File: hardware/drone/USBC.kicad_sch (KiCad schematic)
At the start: 8 parts

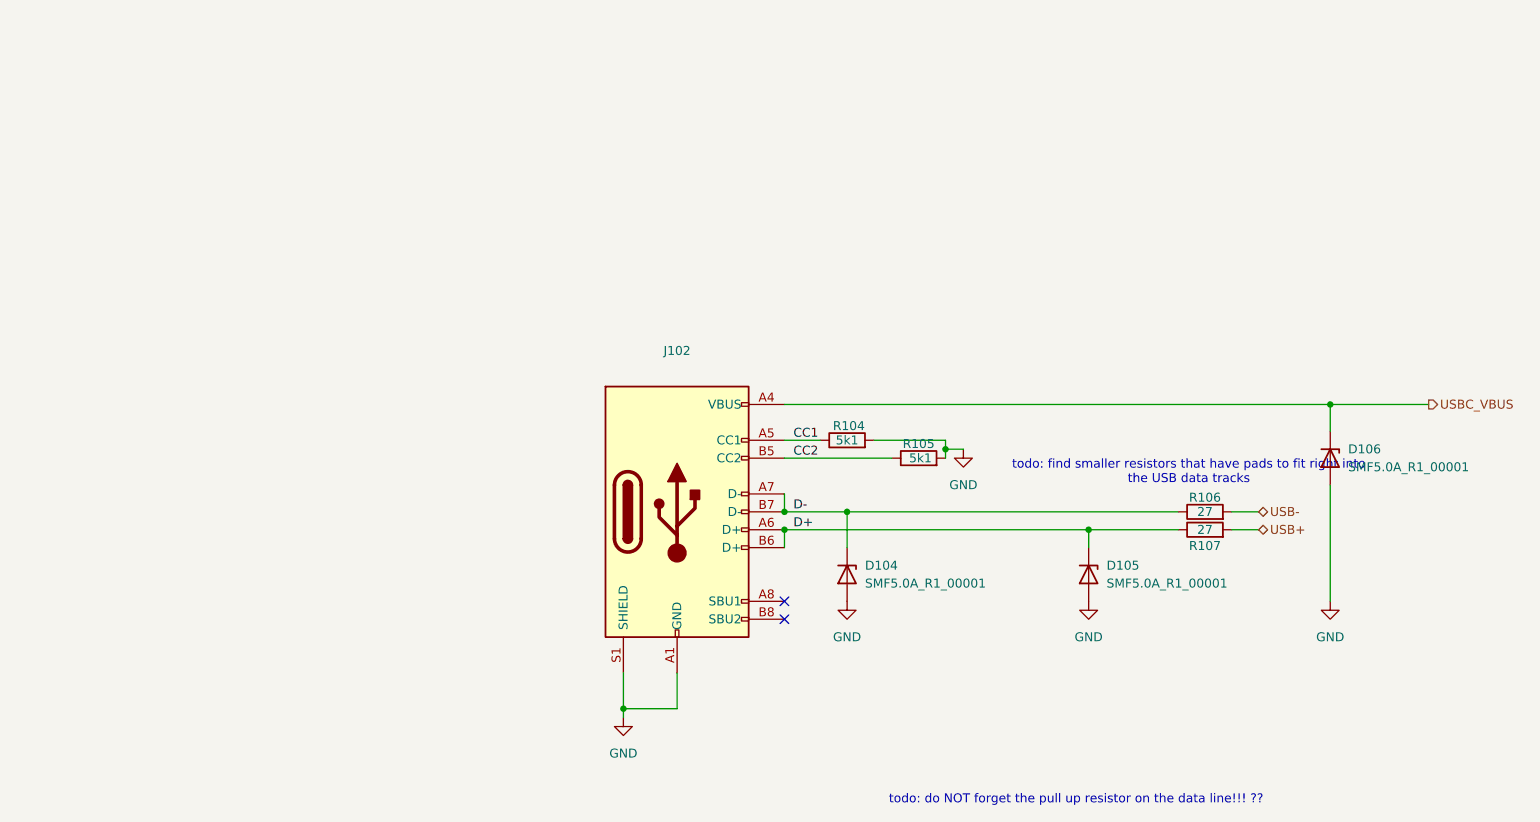
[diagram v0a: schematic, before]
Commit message: save before axing motor driver ic's
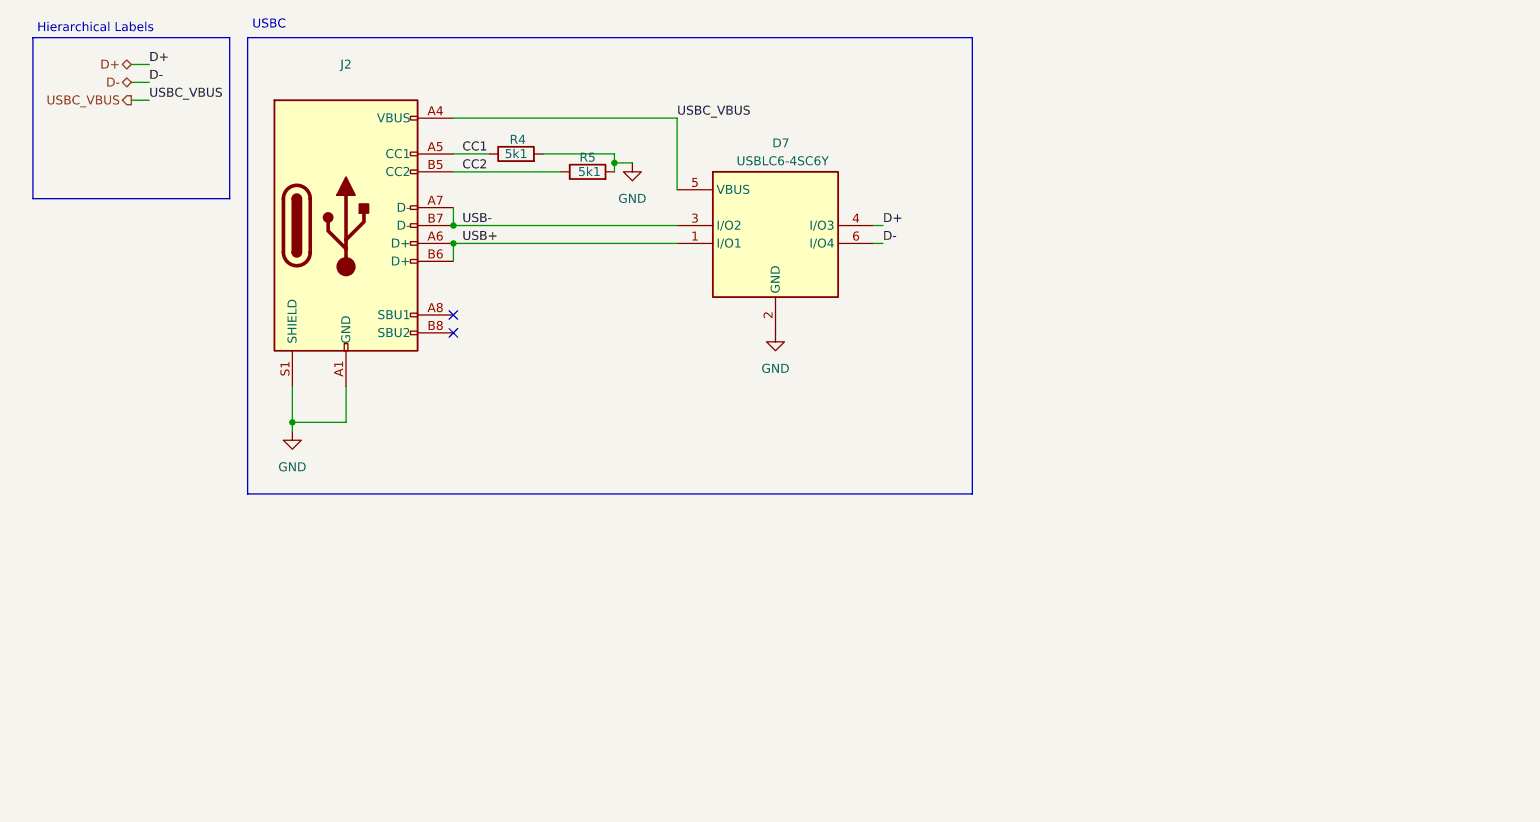
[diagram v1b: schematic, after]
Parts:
- removed D104, D105, D106: SMF5.0A_R1_00001, SamacSys_Parts:SMF50A_R1_00001, symbol Device:D_Zener
- removed R106, R107: 27, SamacSys_Parts:RESC1005X40N, symbol Device:R
- added D7: USBLC6-4SC6Y, SamacSys_Parts:SOT95P280X145-6N, symbol SamacSys_Parts:USBLC6-4SC6Y
- renumbered J102 to J2, R104 to R4, R105 to R5
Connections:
- net D+: now also D7.4 (I/O3); no longer J2.A6 (D+), J2.B6 (D+)
- net D-: now also D7.6 (I/O4); no longer J2.A7 (D-), J2.B7 (D-)
- net GND: now also D7.2 (GND)
- net USB+: now also J2.A6 (D+), J2.B6 (D+), D7.1 (I/O1)
- net USB-: now also J2.A7 (D-), J2.B7 (D-), D7.3 (I/O2)
- net USBC_VBUS: now also D7.5 (VBUS)
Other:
- note added: "Hierarchical Labels"
- note added: "USBC"
- note removed: "todo: do NOT forget the pull up resistor on the data line!!! ??"
- note removed: "todo: find smaller resistors that have pads to fit right into the USB data tracks"
- moved on the sheet: J2, R4, R5

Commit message: axed motor drivers. finished layout for drone but need to review overall system design after reading some stuff
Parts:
- renumbered D7 to D4
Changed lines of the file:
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@@
 		(on_board yes)
 		(dnp no)
-		(property "Reference" "D7"
+		(property "Reference" "D4"
 			(at 120.142 32.766 0)
 			(effects
@@
 			(project ""
 				(path "/869bea87-c885-4ead-826b-3f34ceacafad/26d17bc2-e2ae-44e6-8fc3-d458d6e51b4a"
-					(reference "D7")
+					(reference "D4")
 					(unit 1)
 				)
@@
 		(dnp no)
 		(fields_autoplaced yes)
-		(property "Reference" "#PWR021"
+		(property "Reference" "#PWR023"
 			(at 50.8 80.01 0)
 			(effects
@@
 			(project ""
 				(path "/869bea87-c885-4ead-826b-3f34ceacafad/26d17bc2-e2ae-44e6-8fc3-d458d6e51b4a"
-					(reference "#PWR021")
+					(reference "#PWR023")
 					(unit 1)
 				)
@@
 		(dnp no)
 		(fields_autoplaced yes)
-		(property "Reference" "#PWR023"
+		(property "Reference" "#PWR024"
 			(at 99.06 41.91 0)
 			(effects
@@
 			(project ""
 				(path "/869bea87-c885-4ead-826b-3f34ceacafad/26d17bc2-e2ae-44e6-8fc3-d458d6e51b4a"
-					(reference "#PWR023")
+					(reference "#PWR024")
 					(unit 1)
 				)
@@
 		(dnp no)
 		(fields_autoplaced yes)
-		(property "Reference" "#PWR022"
+		(property "Reference" "#PWR025"
 			(at 119.38 66.04 0)
 			(effects
@@
 			(project "drone"
 				(path "/869bea87-c885-4ead-826b-3f34ceacafad/26d17bc2-e2ae-44e6-8fc3-d458d6e51b4a"
-					(reference "#PWR022")
+					(reference "#PWR025")
 					(unit 1)
 				)
